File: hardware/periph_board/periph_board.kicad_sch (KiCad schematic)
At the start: 21 parts, among them IC100 ADC081S021CIMF_NOPB, IC101 CD74HC4067SM96, J100 2x9 Male Pins

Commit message: layout with bad adc
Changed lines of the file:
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@@
 		(dnp no)
 		(property "Reference" "C101"
-			(at 185.674 75.692 0)
+			(at 187.96 73.152 0)
 			(effects
 				(font
@@
 		)
 		(property "Value" "1u"
-			(at 185.674 73.152 0)
+			(at 186.944 75.692 0)
 			(effects
 				(font
@@
 		(dnp no)
 		(property "Reference" "C100"
+			(at 201.93 34.544 0)
+			(effects
+				(font
+					(size 1.27 1.27)
+				)
+				(justify left)
+			)
+		)
+		(property "Value" "1u"
 			(at 201.93 37.084 0)
 			(effects
 				(font
-					(size 1.27 1.27)
-				)
-				(justify left)
-			)
-		)
-		(property "Value" "1u"
-			(at 201.93 34.544 0)
-			(effects
-				(font

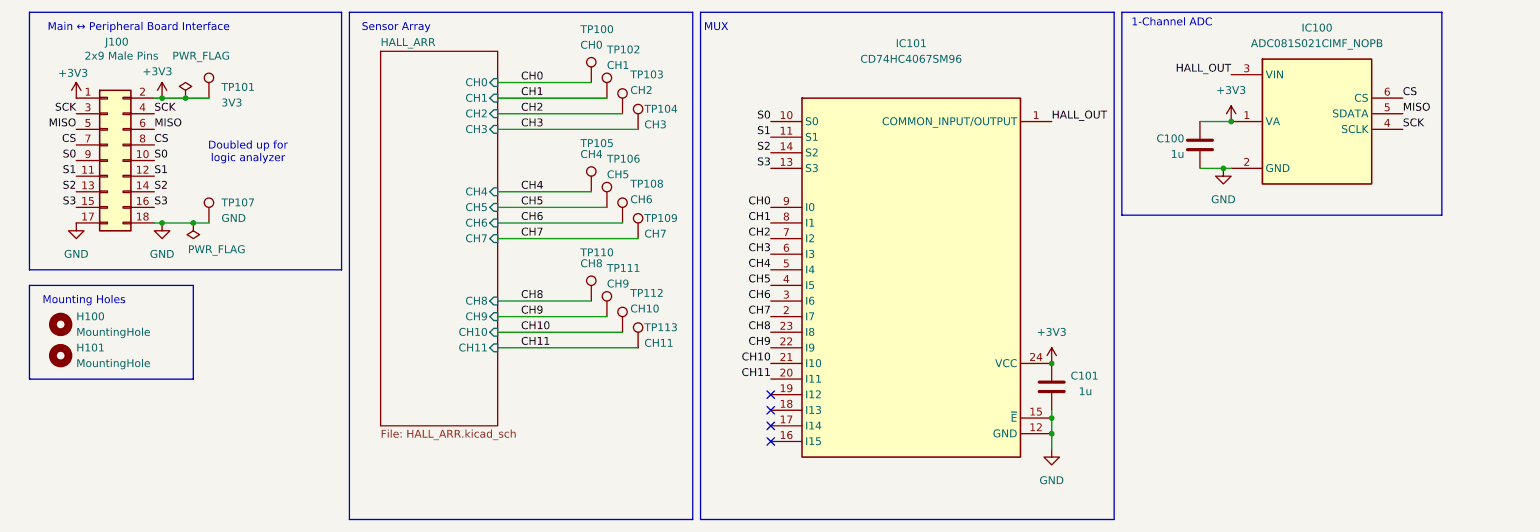
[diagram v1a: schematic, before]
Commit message: ece445l libraries added. moved mspm0 starter to /hw to /hardware with other files
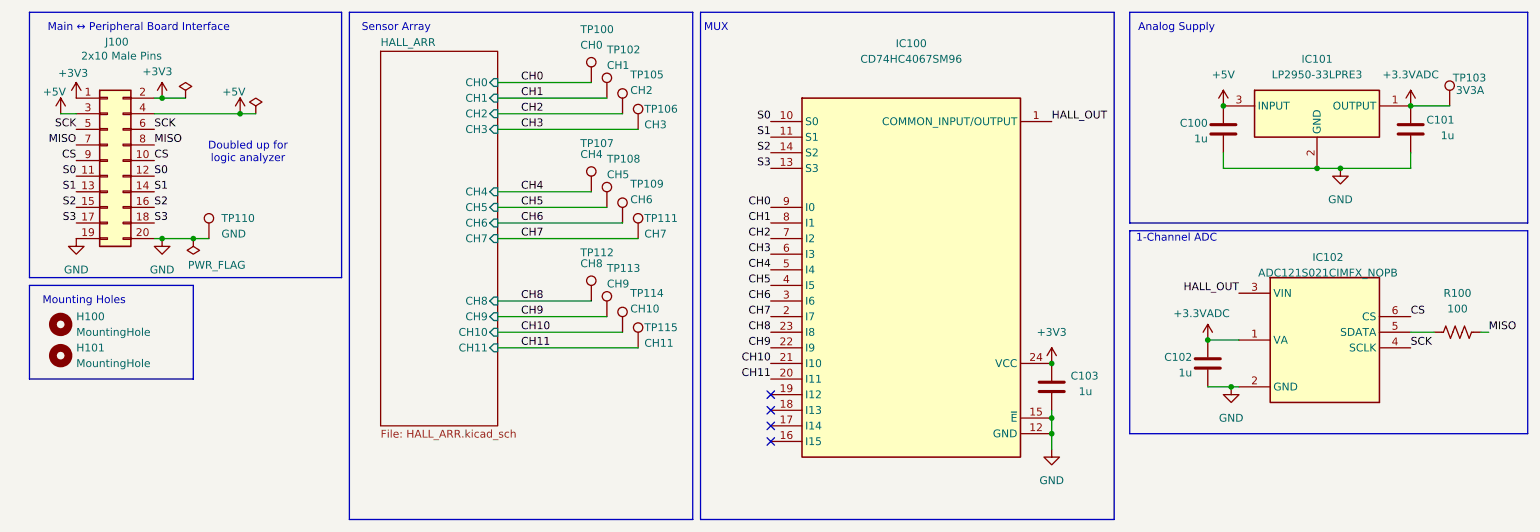
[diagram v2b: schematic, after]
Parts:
- removed IC100: ADC081S021CIMF_NOPB, SOT95P280X145-6N, symbol SamacSys_Parts:ADC081S021CIMF_NOPB
- removed TP101: 3V3, SamacSys_Parts:bettertestpoint2, symbol Connector:TestPoint
- added C100, C101: 1u, Capacitor_SMD:C_0805_2012Metric_Pad1.18x1.45mm_HandSolder, symbol Device:C
- added IC101: LP2950-33LPRE3, 445L:TL431CLPM, symbol LP2950-33LPRE3:LP2950-33LPRE3
- added IC102: ADC121S021CIMFX_NOPB, SOT95P280X145-6N, symbol SamacSys_Parts:ADC121S021CIMFX_NOPB
- added R100: 100, Resistor_SMD:R_0805_2012Metric, symbol Device:R_US
- added TP103: 3V3A, SamacSys_Parts:bettertestpoint2, symbol Connector:TestPoint
- J100: value 2x9 Male Pins -> 2x10 Male Pins; footprint Connector_PinSocket_2.54mm:PinSocket_2x09_P2.54mm_Vertical -> Connector_PinSocket_2.54mm:PinSocket_2x10_P2.54mm_Vertical; symbol Connector_Generic:Conn_02x09_Odd_Even -> Connector_Generic:Conn_02x10_Odd_Even
- renumbered C100 to C102, C101 to C103, IC101 to IC100, TP103 to TP105, TP104 to TP106, TP105 to TP107, TP106 to TP108, TP108 to TP109, TP107 to TP110, TP109 to TP111, TP110 to TP112, TP111 to TP113, TP112 to TP114, TP113 to TP115
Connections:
- net +3V3: no longer C102.2
- net CS: now also J100.10 (Pin_10), J100.9 (Pin_9), IC102.6 (CS); no longer J100.7 (Pin_7), J100.8 (Pin_8)
- net GND: now also J100.19 (Pin_19), J100.20 (Pin_20), C100.1, C101.1, IC101.2 (GND), IC102.2 (GND); no longer J100.17 (Pin_17), J100.18 (Pin_18)
- net HALL_OUT: now also IC102.3 (VIN)
- net MISO: now also J100.7 (Pin_7), J100.8 (Pin_8), R100.2; no longer J100.5 (Pin_5), J100.6 (Pin_6)
- net S0: now also J100.11 (Pin_11), J100.12 (Pin_12); no longer J100.10 (Pin_10), J100.9 (Pin_9)
- net S1: now also J100.13 (Pin_13), J100.14 (Pin_14); no longer J100.11 (Pin_11), J100.12 (Pin_12)
- net S2: now also J100.15 (Pin_15), J100.16 (Pin_16); no longer J100.13 (Pin_13), J100.14 (Pin_14)
- net S3: now also J100.17 (Pin_17), J100.18 (Pin_18); no longer J100.15 (Pin_15), J100.16 (Pin_16)
- net SCK: now also J100.5 (Pin_5), J100.6 (Pin_6), IC102.4 (SCLK); no longer J100.3 (Pin_3), J100.4 (Pin_4)
- new net: IC102.5 (SDATA), R100.1
- new net +3.3VADC: C101.2, C102.2, IC101.1 (OUTPUT), IC102.1 (VA), TP103.1
- new net +5V: C100.2, IC101.3 (INPUT), J100.3 (Pin_3), J100.4 (Pin_4)
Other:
- note added: "Analog Supply"
- moved on the sheet: C102, TP110
